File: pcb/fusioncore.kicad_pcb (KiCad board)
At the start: 2 copper layers, 95 x 99 mm, 123 parts, among them J1 40HAT, J10 Pump_Misc_1, J11 Pump_Misc_2, J12 I2C_DBG, J13 Conn_02x03_Top_Bottom, J14 LED, J15 Trigger, J16 WEIGHT, J17 Valve_M1, J18 Valve_M2, J19 Valve_M3, J2 Conn_02x12_Top_Bottom, J20 Valve_M4, J21 Valve_Air_Lime, J22 Valve_Air_Rum, J23 Valve_Air_Out, J24 Cooling_Copressor, J3 Flow_Warm, J4 Temperature, J5 Flow_Cold, J6 WEIGHT_B, J7 Pump_Cold, J8 Pump_Warm, J9 Pump_Air, K1 G5Q-1A, Q1 DMG2305UX, Q10 AO3400A, Q11 AO3400A, Q12 2N3904, Q2 DMMT5401, Q3 AO3400A, Q4 AO3400A, Q5 AO3400A, Q6 AO3400A, Q7 AO3400A, Q8 MMBT4403, Q9 AO3400A, SW1 POWER_ON, U1 CAT24C32, U2 INA226, U3 INA226, U4 INA226, U5 TXB0108DQSR, U6 HX711, U7 P82B96

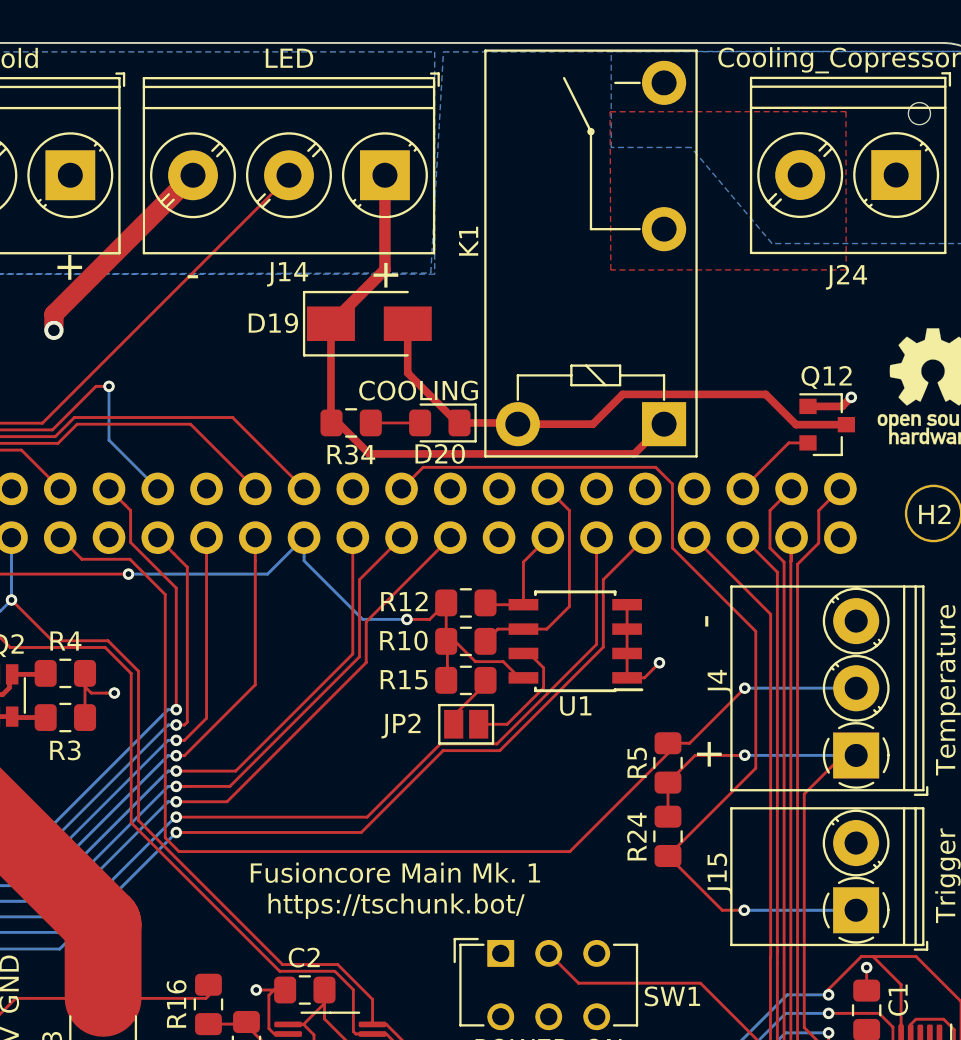
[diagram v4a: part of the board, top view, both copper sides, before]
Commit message: Added Relais to board
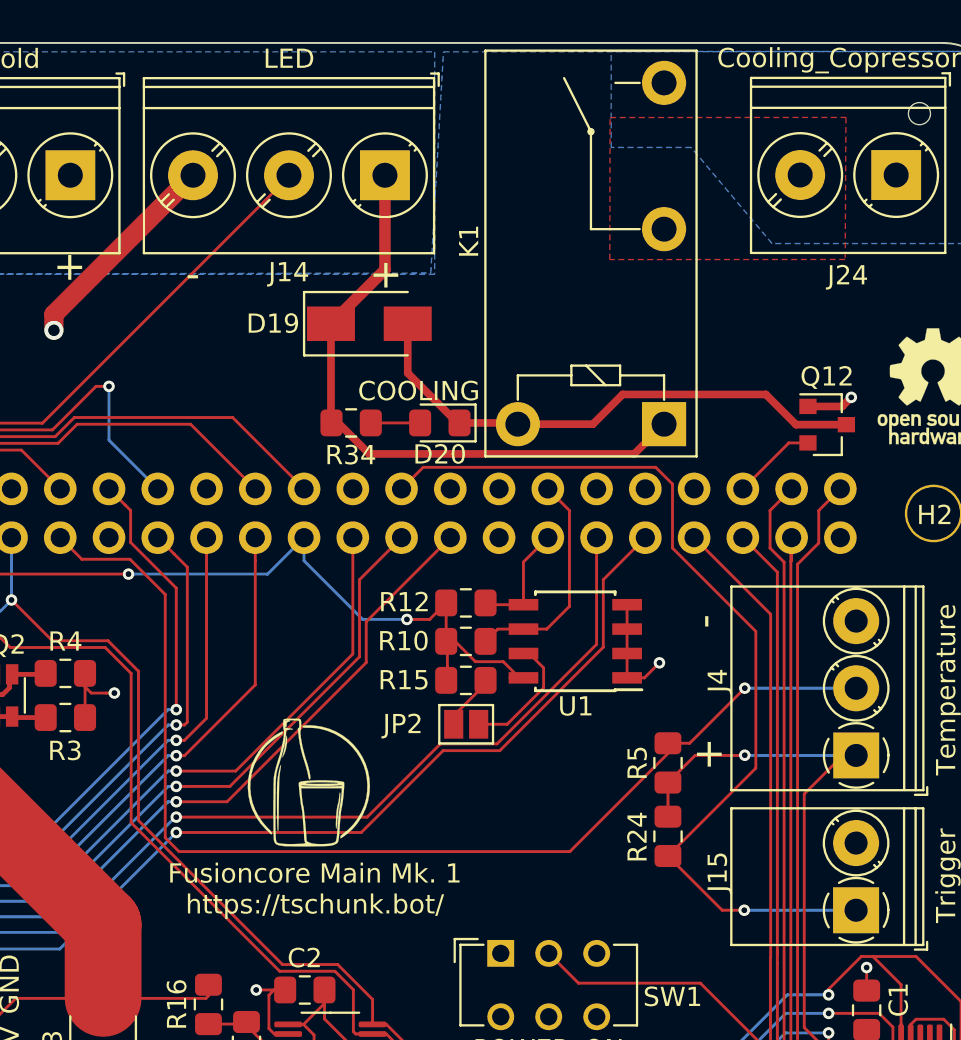
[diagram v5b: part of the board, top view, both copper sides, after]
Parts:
- added G***: LOGO, project_footprints:fusioncore_logo, F.Cu at (107.5, 78.1)

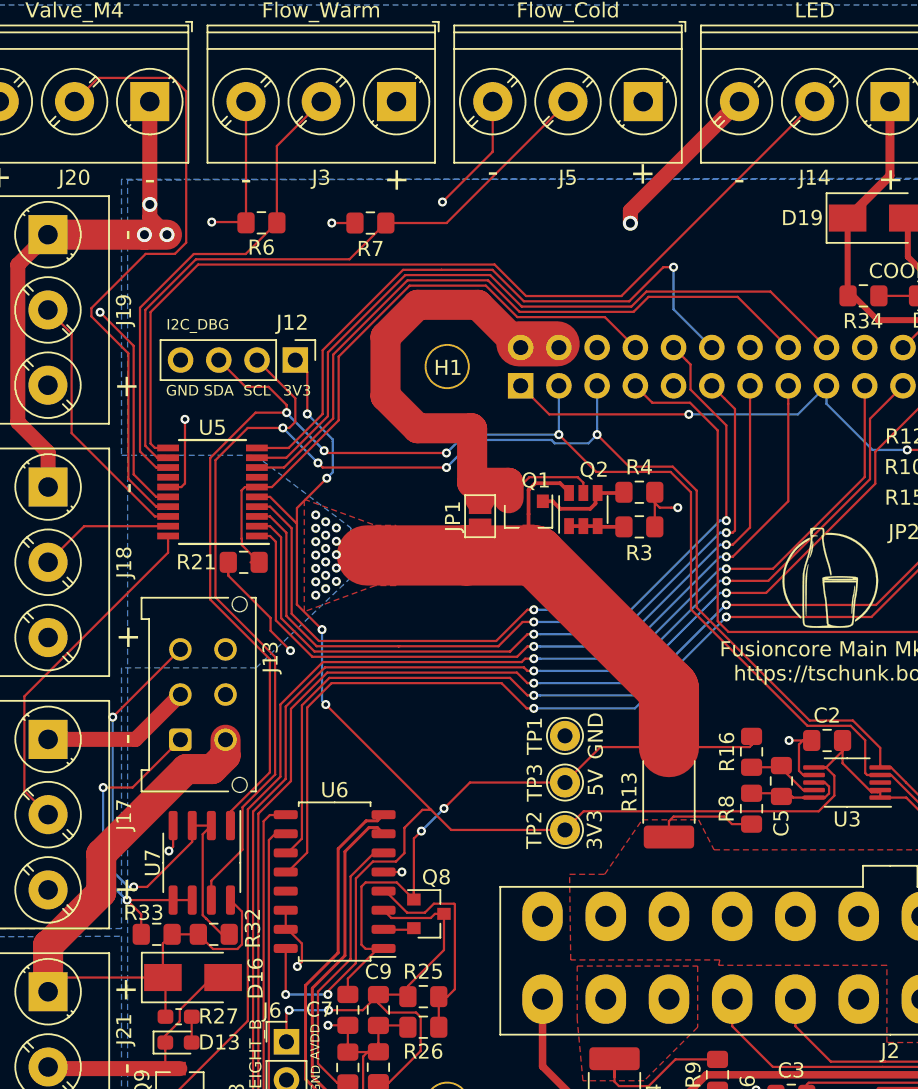
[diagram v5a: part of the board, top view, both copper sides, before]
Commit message: Simplified some layouts
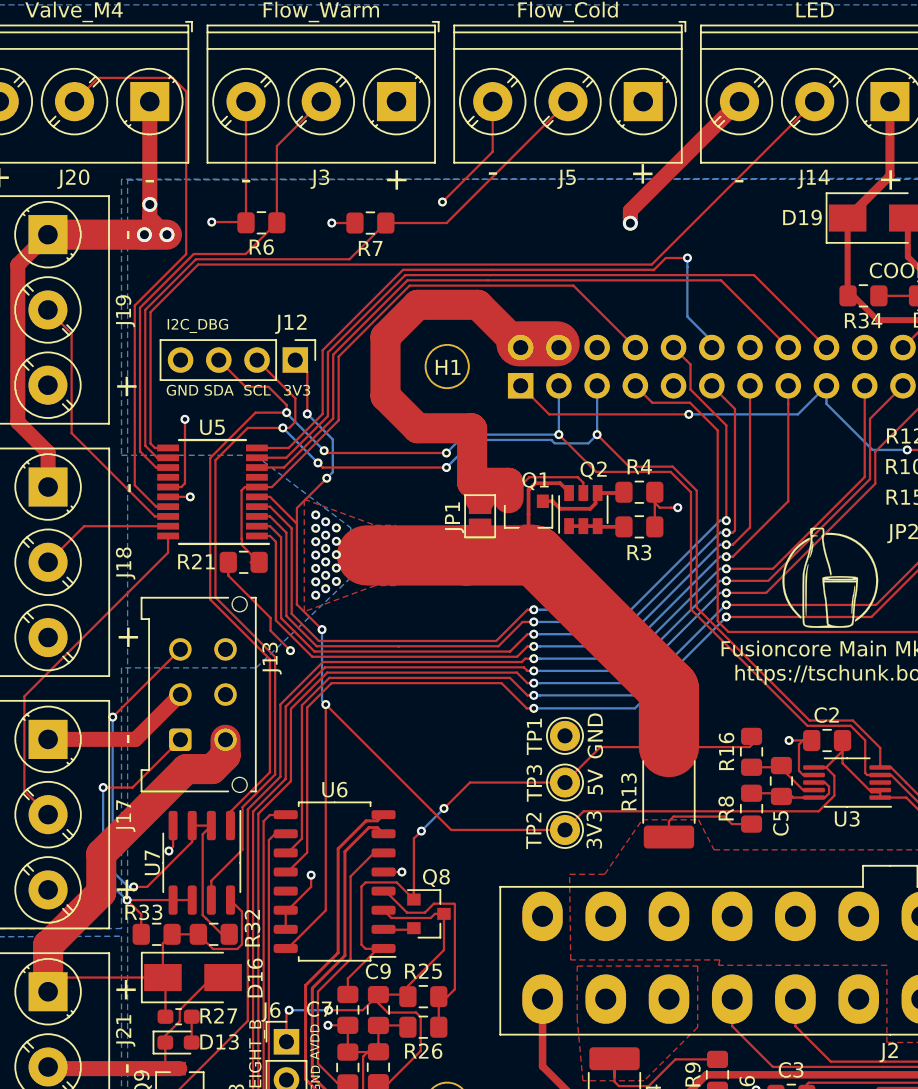
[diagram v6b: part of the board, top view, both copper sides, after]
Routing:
- net /5V: track 124.8 -> 111.7 mm
- net /3V3: track 240.9 -> 236.0 mm, vias 11 -> 9
- net /Valve_M4_5V: track 42.3 -> 38.8 mm
- net /LED_PWM_5V: track 61.7 -> 60.0 mm
- net /Flow_C: track 48.2 -> 47.3 mm
- net /Flow_W: track 45.6 -> 44.8 mm
